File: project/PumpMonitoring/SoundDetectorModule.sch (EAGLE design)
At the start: 32 parts, among them CN1 JST-PH-K*, IC1 LMV324

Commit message: modify schematic of sound detect module.
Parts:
- added C5, C6: NC, SparkFun-Capacitors:10UF-6.3V-20%(1206)
- added R22: NC, SparkFun-Resistors:1KOHM1/10W1%(0603)
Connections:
- new net N$13: C5.2
- net GND: now also C5.1, C6.1
- net N$2: now also C6.2, R22.2
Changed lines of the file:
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@@
 <?xml version="1.0" encoding="utf-8"?>
 <!DOCTYPE eagle SYSTEM "eagle.dtd">
-<eagle version="7.7.0">
+<eagle version="7.6.0">
 <drawing>
 <settings>
@@
 <part name="R20" library="resistor" deviceset="R-US_" device="0207/7" value="0"/>
 <part name="R21" library="resistor" deviceset="R-US_" device="0207/7" value="0"/>
+<part name="C5" library="SparkFun-Capacitors" deviceset="10UF-6.3V-20%(1206)" device="" value="NC"/>
+<part name="R22" library="SparkFun-Resistors" deviceset="1KOHM1/10W1%(0603)" device="" value="NC"/>
+<part name="C6" library="SparkFun-Capacitors" deviceset="10UF-6.3V-20%(1206)" device="" value="NC"/>
 </parts>
 <sheets>
@@
 <instance part="R20" gate="G$1" x="154.94" y="198.12"/>
 <instance part="R21" gate="G$1" x="215.9" y="190.5"/>
+<instance part="C5" gate="G$1" x="119.38" y="152.4" rot="R90"/>
+<instance part="R22" gate="G$1" x="129.54" y="152.4"/>
+<instance part="C6" gate="G$1" x="144.78" y="149.86" rot="R180"/>
 </instances>
 <busses>
@@
 <pinref part="GND3" gate="1" pin="GND"/>
 <wire x1="137.16" y1="142.24" x2="137.16" y2="139.7" width="0.1524" layer="91"/>
+<pinref part="C6" gate="G$1" pin="1"/>
+<wire x1="137.16" y1="142.24" x2="144.78" y2="142.24" width="0.1524" layer="91"/>
+<wire x1="144.78" y1="142.24" x2="144.78" y2="144.78" width="0.1524" layer="91"/>
+<junction x="137.16" y="142.24"/>
 </segment>
 <segment>
@@
 <pinref part="GND2" gate="1" pin="GND"/>
 <wire x1="109.22" y1="157.48" x2="109.22" y2="139.7" width="0.1524" layer="91"/>
+<pinref part="C5" gate="G$1" pin="1"/>
+<wire x1="109.22" y1="157.48" x2="114.3" y2="157.48" width="0.1524" layer="91"/>
+<wire x1="114.3" y1="157.48" x2="114.3" y2="152.4" width="0.1524" layer="91"/>
+<junction x="109.22" y="157.48"/>
 </segment>
 <segment>
@@
 <wire x1="144.78" y1="154.94" x2="137.16" y2="154.94" width="0.1524" layer="91"/>
 <junction x="137.16" y="154.94"/>
+<pinref part="R22" gate="G$1" pin="2"/>
+<wire x1="134.62" y1="152.4" x2="134.62" y2="154.94" width="0.1524" layer="91"/>
+<wire x1="134.62" y1="154.94" x2="137.16" y2="154.94" width="0.1524" layer="91"/>
+<pinref part="C6" gate="G$1" pin="2"/>
+<wire x1="144.78" y1="152.4" x2="137.16" y2="152.4" width="0.1524" layer="91"/>
+<junction x="137.16" y="152.4"/>
 </segment>
 </net>
@@
 </segment>
 </net>
+<net name="N$13" class="0">
+<segment>
+<pinref part="C5" gate="G$1" pin="2"/>
+<wire x1="121.92" y1="152.4" x2="127" y2="152.4" width="0.1524" layer="91"/>
+</segment>
+</net>

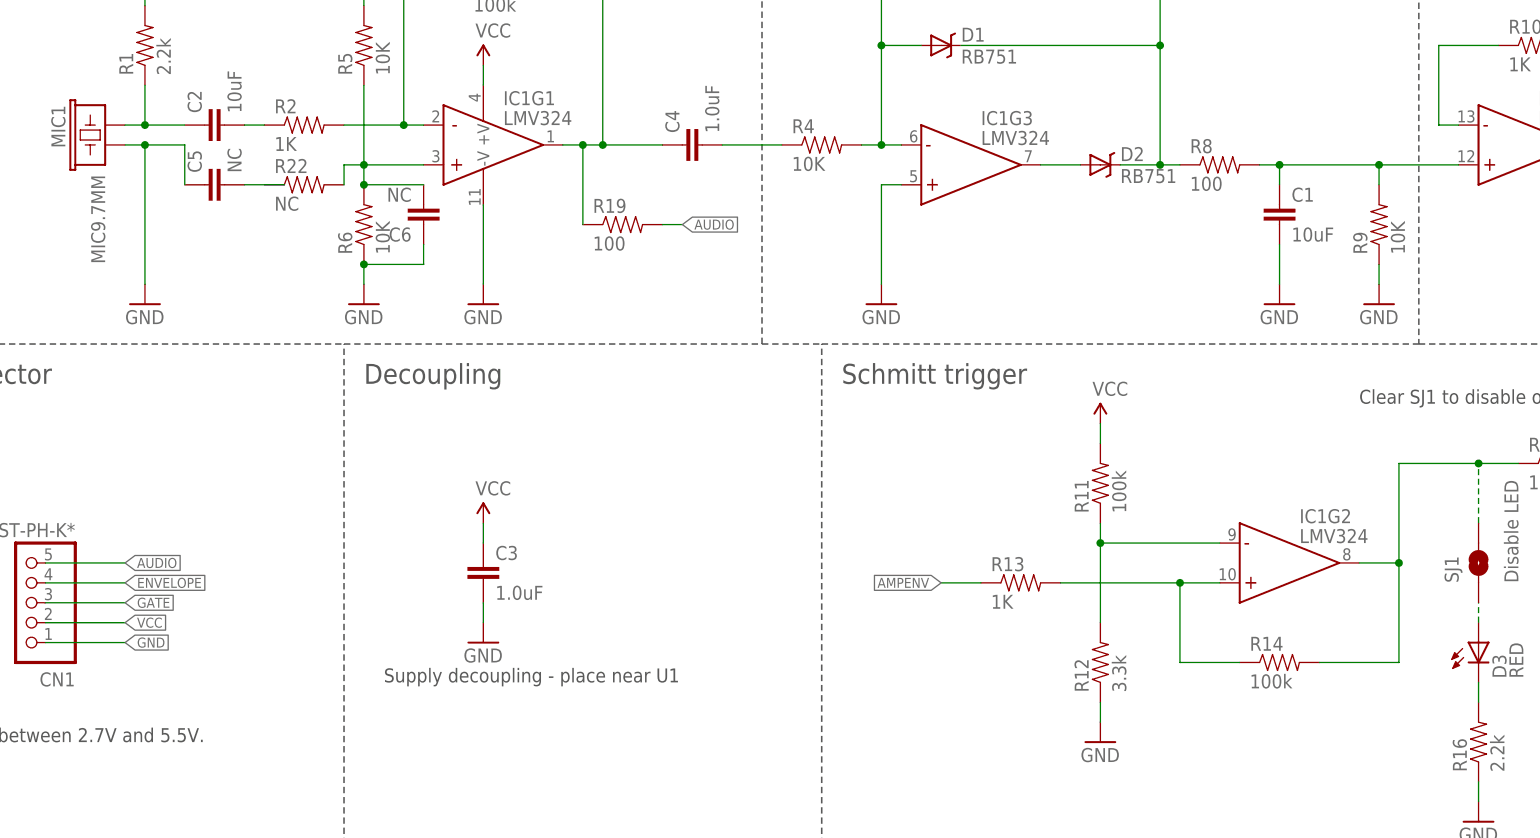
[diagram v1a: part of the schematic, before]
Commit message: update sound detector module
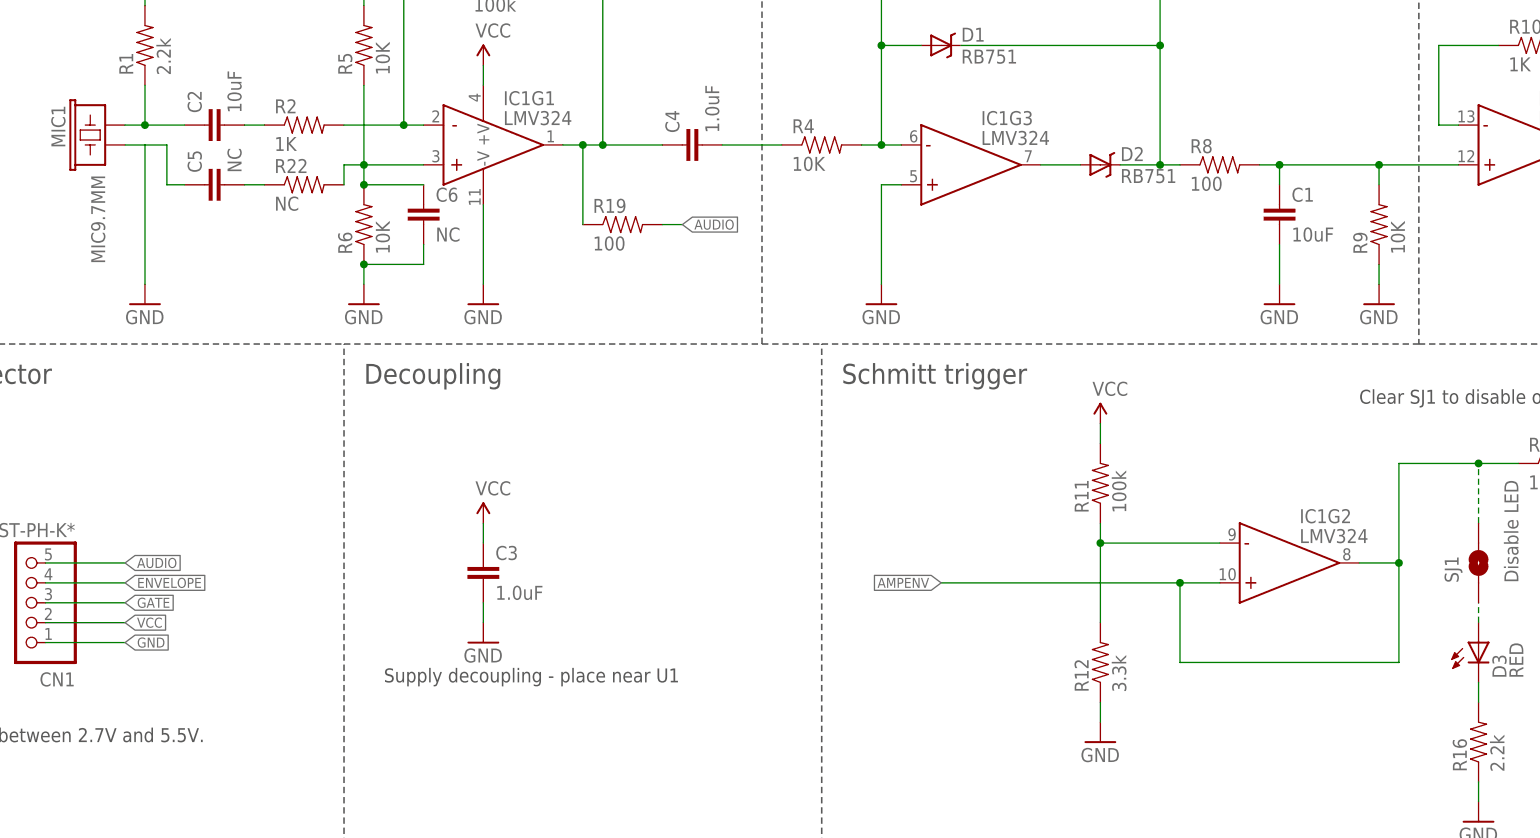
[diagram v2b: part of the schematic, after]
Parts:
- removed R13: 1K, SparkFun-Resistors:1KOHM1/10W1%(0603)
- removed R14: 100k, SparkFun-Resistors:100KOHM1/10W1%(0603)
- C5, C6: device SparkFun-Capacitors:10UF-6.3V-20%(1206) -> SparkFun-Capacitors:1.0UF-16V-10%(0603)
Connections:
- removed net N$16: IC1G2.+IN, R13.2, R14.1
- removed net N$17: IC1G2.OUT, R14.2, R15.1, SJ1.2
- net AMPENV: now also IC1G2.+IN, IC1G2.OUT, R15.1, SJ1.2; no longer R13.1
- net GND: now also C6.2; no longer C6.1
- net N$13: now also R22.1
- net N$2: now also C6.1; no longer C6.2
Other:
- moved on the sheet: C6
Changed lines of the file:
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@@
 <?xml version="1.0" encoding="utf-8"?>
 <!DOCTYPE eagle SYSTEM "eagle.dtd">
-<eagle version="7.6.0">
+<eagle version="7.7.0">
 <drawing>
 <settings>
@@
 <part name="R11" library="SparkFun-Resistors" deviceset="100KOHM1/10W1%(0603)" device="" value="100k"/>
 <part name="R12" library="SparkFun-Resistors" deviceset="3.3KOHM1/10W1%(0603)" device="" value="3.3k"/>
-<part name="R13" library="SparkFun-Resistors" deviceset="1KOHM1/10W1%(0603)" device="" value="1K"/>
-<part name="R14" library="SparkFun-Resistors" deviceset="100KOHM1/10W1%(0603)" device="" value="100k"/>
 <part name="SUPPLY4" library="SparkFun-Aesthetics" deviceset="VCC" device=""/>
 <part name="GND8" library="SparkFun-Aesthetics" deviceset="GND" device=""/>
@@
 <part name="R20" library="resistor" deviceset="R-US_" device="0207/7" value="0"/>
 <part name="R21" library="resistor" deviceset="R-US_" device="0207/7" value="0"/>
-<part name="C5" library="SparkFun-Capacitors" deviceset="10UF-6.3V-20%(1206)" device="" value="NC"/>
 <part name="R22" library="SparkFun-Resistors" deviceset="1KOHM1/10W1%(0603)" device="" value="NC"/>
-<part name="C6" library="SparkFun-Capacitors" deviceset="10UF-6.3V-20%(1206)" device="" value="NC"/>
+<part name="C5" library="SparkFun-Capacitors" deviceset="1.0UF-16V-10%(0603)" device="" value="NC"/>
+<part name="C6" library="SparkFun-Capacitors" deviceset="1.0UF-16V-10%(0603)" device="" value="NC"/>
 </parts>
 <sheets>
@@
 <instance part="R11" gate="G$1" x="231.14" y="114.3" rot="R90"/>
 <instance part="R12" gate="G$1" x="231.14" y="91.44" rot="R90"/>
-<instance part="R13" gate="G$1" x="220.98" y="101.6"/>
-<instance part="R14" gate="G$1" x="254" y="91.44"/>
 <instance part="SUPPLY4" gate="1" x="231.14" y="121.92"/>
 <instance part="GND8" gate="1" x="231.14" y="81.28"/>
@@
 <instance part="R20" gate="G$1" x="154.94" y="198.12"/>
 <instance part="R21" gate="G$1" x="215.9" y="190.5"/>
+<instance part="R22" gate="G$1" x="129.54" y="152.4"/>
 <instance part="C5" gate="G$1" x="119.38" y="152.4" rot="R90"/>
-<instance part="R22" gate="G$1" x="129.54" y="152.4"/>
-<instance part="C6" gate="G$1" x="144.78" y="149.86" rot="R180"/>
+<instance part="C6" gate="G$1" x="144.78" y="147.32"/>
 </instances>
 <busses>
@@
 <pinref part="GND3" gate="1" pin="GND"/>
 <wire x1="137.16" y1="142.24" x2="137.16" y2="139.7" width="0.1524" layer="91"/>
-<pinref part="C6" gate="G$1" pin="1"/>
 <wire x1="137.16" y1="142.24" x2="144.78" y2="142.24" width="0.1524" layer="91"/>
 <wire x1="144.78" y1="142.24" x2="144.78" y2="144.78" width="0.1524" layer="91"/>
 <junction x="137.16" y="142.24"/>
+<pinref part="C6" gate="G$1" pin="2"/>
 </segment>
 <segment>
@@
 <pinref part="GND2" gate="1" pin="GND"/>
 <wire x1="109.22" y1="157.48" x2="109.22" y2="139.7" width="0.1524" layer="91"/>
+<wire x1="109.22" y1="157.48" x2="112.014" y2="157.48" width="0.1524" layer="91"/>
+<wire x1="112.014" y1="157.48" x2="112.014" y2="152.4" width="0.1524" layer="91"/>
+<wire x1="112.014" y1="152.4" x2="114.3" y2="152.4" width="0.1524" layer="91"/>
 <pinref part="C5" gate="G$1" pin="1"/>
-<wire x1="109.22" y1="157.48" x2="114.3" y2="157.48" width="0.1524" layer="91"/>
-<wire x1="114.3" y1="157.48" x2="114.3" y2="152.4" width="0.1524" layer="91"/>
-<junction x="109.22" y="157.48"/>
 </segment>
 <segment>
@@
 <wire x1="144.78" y1="154.94" x2="137.16" y2="154.94" width="0.1524" layer="91"/>
 <junction x="137.16" y="154.94"/>
-<pinref part="R22" gate="G$1" pin="2"/>
-<wire x1="134.62" y1="152.4" x2="134.62" y2="154.94" width="0.1524" layer="91"/>
 <wire x1="134.62" y1="154.94" x2="137.16" y2="154.94" width="0.1524" layer="91"/>
-<pinref part="C6" gate="G$1" pin="2"/>
 <wire x1="144.78" y1="152.4" x2="137.16" y2="152.4" width="0.1524" layer="91"/>
 <junction x="137.16" y="152.4"/>
+<pinref part="R22" gate="G$1" pin="2"/>
+<wire x1="134.62" y1="154.94" x2="134.62" y2="152.4" width="0.1524" layer="91"/>
+<pinref part="C6" gate="G$1" pin="1"/>
 </segment>
 </net>
@@
 </segment>
 <segment>
-<pinref part="R13" gate="G$1" pin="1"/>
-<wire x1="215.9" y1="101.6" x2="210.82" y2="101.6" width="0.1524" layer="91"/>
 <label x="210.82" y="101.6" size="1.27" layer="95" rot="R180" xref="yes"/>
-</segment>
-</net>
-<net name="N$15" class="0">
-<segment>
-<pinref part="R11" gate="G$1" pin="1"/>
-<pinref part="R12" gate="G$1" pin="2"/>
-<wire x1="231.14" y1="109.22" x2="231.14" y2="106.68" width="0.1524" layer="91"/>
-<pinref part="IC1" gate="G2" pin="-IN"/>
-<wire x1="231.14" y1="106.68" x2="231.14" y2="96.52" width="0.1524" layer="91"/>
-<wire x1="246.38" y1="106.68" x2="231.14" y2="106.68" width="0.1524" layer="91"/>
-<junction x="231.14" y="106.68"/>
-</segment>
-</net>
-<net name="N$16" class="0">
-<segment>
-<pinref part="R13" gate="G$1" pin="2"/>
-<wire x1="241.3" y1="101.6" x2="226.06" y2="101.6" width="0.1524" layer="91"/>
 <wire x1="241.3" y1="101.6" x2="241.3" y2="91.44" width="0.1524" layer="91"/>
-<pinref part="R14" gate="G$1" pin="1"/>
-<wire x1="241.3" y1="91.44" x2="248.92" y2="91.44" width="0.1524" layer="91"/>
 <pinref part="IC1" gate="G2" pin="+IN"/>
 <wire x1="246.38" y1="101.6" x2="241.3" y2="101.6" width="0.1524" layer="91"/>
 <junction x="241.3" y="101.6"/>
-</segment>
-</net>
-<net name="N$17" class="0">
-<segment>
-<pinref part="R14" gate="G$1" pin="2"/>
-<wire x1="259.08" y1="91.44" x2="269.24" y2="91.44" width="0.1524" layer="91"/>
+<wire x1="210.82" y1="101.6" x2="241.3" y2="101.6" width="0.1524" layer="91"/>
 <wire x1="269.24" y1="91.44" x2="269.24" y2="104.14" width="0.1524" layer="91"/>
 <pinref part="IC1" gate="G2" pin="OUT"/>
@@
 <wire x1="279.4" y1="109.22" x2="279.4" y2="116.84" width="0.1524" layer="91" style="longdash"/>
 <junction x="279.4" y="116.84"/>
+<wire x1="241.3" y1="91.44" x2="269.24" y2="91.44" width="0.1524" layer="91"/>
+</segment>
+</net>
+<net name="N$15" class="0">
+<segment>
+<pinref part="R11" gate="G$1" pin="1"/>
+<pinref part="R12" gate="G$1" pin="2"/>
+<wire x1="231.14" y1="109.22" x2="231.14" y2="106.68" width="0.1524" layer="91"/>
+<pinref part="IC1" gate="G2" pin="-IN"/>
+<wire x1="231.14" y1="106.68" x2="231.14" y2="96.52" width="0.1524" layer="91"/>
+<wire x1="246.38" y1="106.68" x2="231.14" y2="106.68" width="0.1524" layer="91"/>
+<junction x="231.14" y="106.68"/>
 </segment>
 </net>
@@
 <net name="N$13" class="0">
 <segment>
+<pinref part="R22" gate="G$1" pin="1"/>
+<wire x1="121.92" y1="152.4" x2="124.46" y2="152.4" width="0.1524" layer="91"/>
 <pinref part="C5" gate="G$1" pin="2"/>
-<wire x1="121.92" y1="152.4" x2="127" y2="152.4" width="0.1524" layer="91"/>
-</segment>
-</net>
+</segment>
+</net>
